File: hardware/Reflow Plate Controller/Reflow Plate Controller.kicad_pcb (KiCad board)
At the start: 4 copper layers, 95 x 43 mm, 86 parts, among them J1 SWD, J2 USB_C_Receptacle_USB2.0_16P, J3 JST-XH, J4 OLED, J5 XT30, J6 XT30, Q1 AO4262E, Q2 SUD50P06-15, Q3 BSS138, SW1 SW_SPST, SW2 SW_SPST, SW3 SW_SPST, SW4 SW_SPST, SW5 SW_SPST, SW6 SW_SPST, SW7 SW_SPST, U1 L78L12ABU, U2 TPS560430, U3 STM32G431KBTx, U4 D5V0P4UR6SO-7, U5 TPD6S300A, U6 UCC27511ADBV

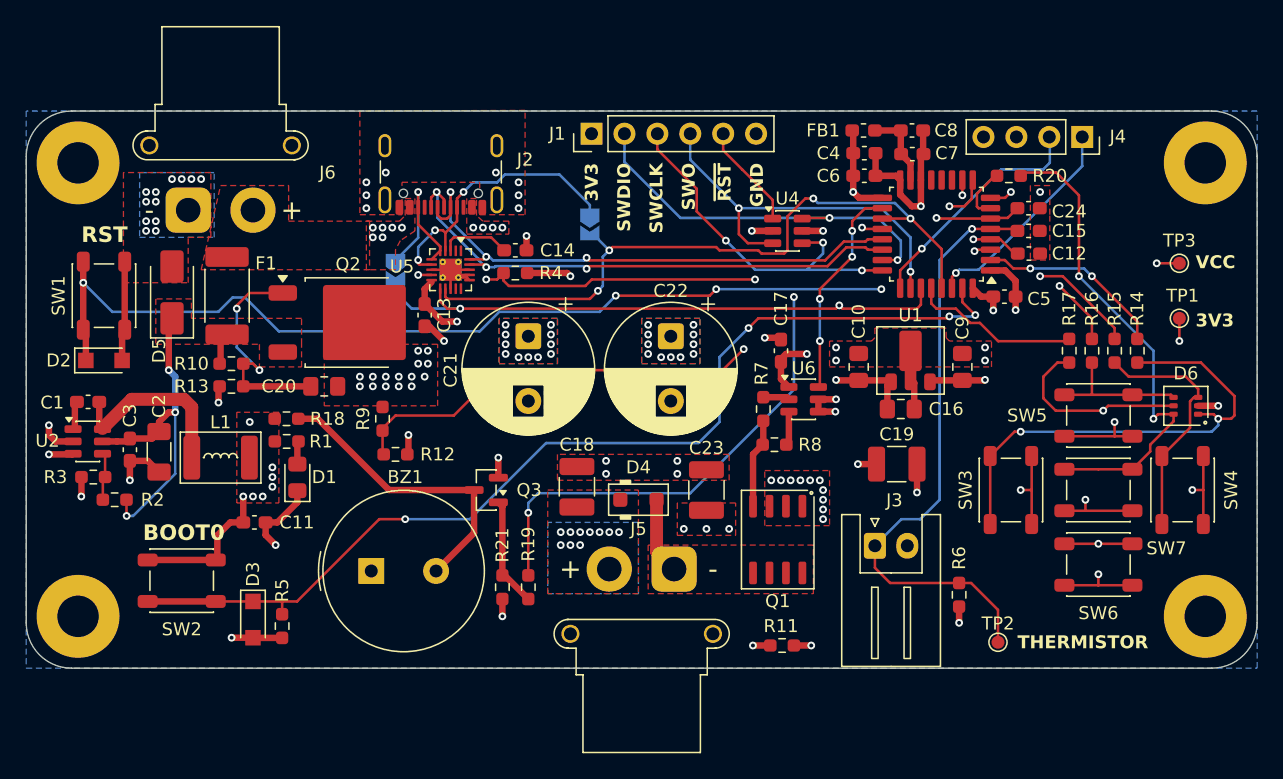
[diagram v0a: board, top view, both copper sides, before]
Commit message: Fix a few layout and component selection issues
- Replace out-of-stock components
- Remove some of the 100nF caps that are in parallel with a larger value
- Swap PTVS3V3 -> SD03
- Swap the PMOS to HSU6119 and the NMOS to DOD130N06 for lower Rds(on)
- Slightly increase the copper area around the FETs
- Reduce the soft-start duration to 47 ms
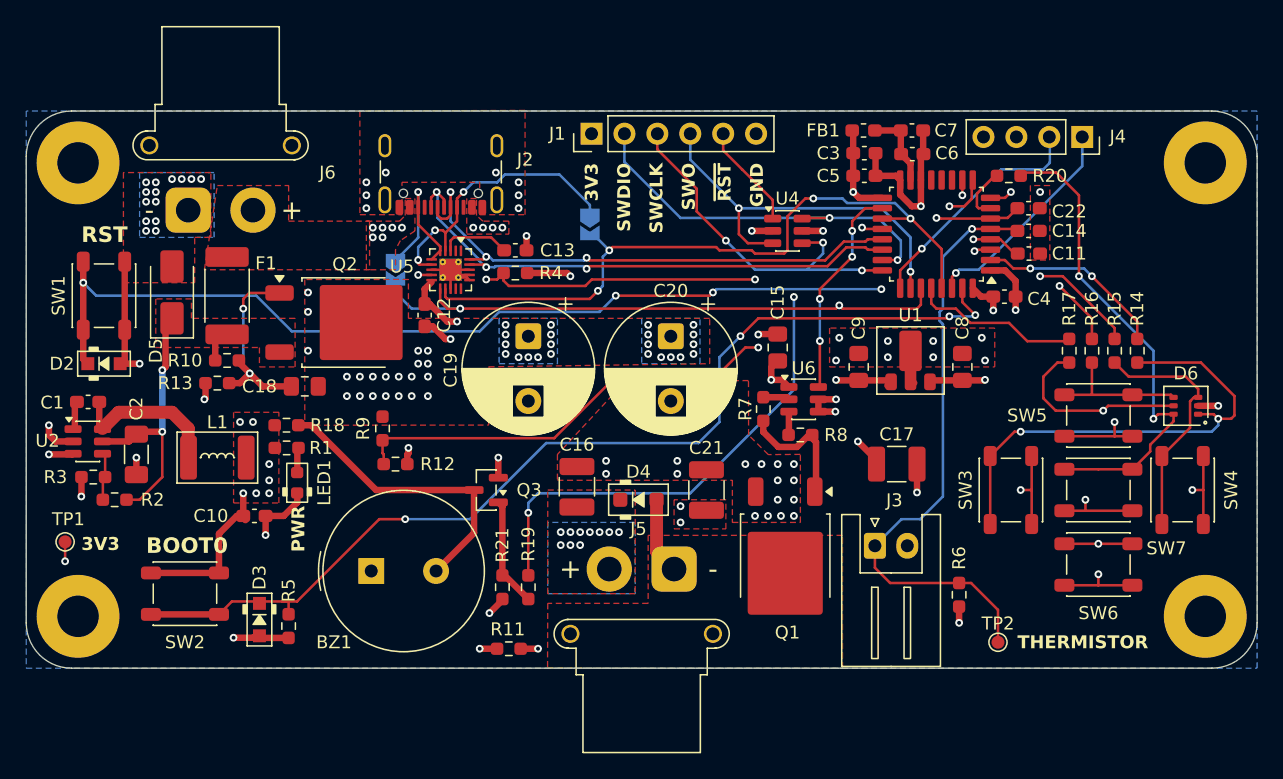
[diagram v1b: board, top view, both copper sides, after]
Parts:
- removed the C16 at (166.0, 101.2)
- removed the C17 at (156.8, 96.8)
- removed the C3 at (106.5, 104.4)
- removed D1: RED, LED_SMD:LED_0805_2012Metric_Pad1.15x1.40mm_HandSolder
- removed TP3: TestPoint, TestPoint:TestPoint_Pad_D1.0mm
- added C15: 2.2u, Capacitor_SMD:C_0805_2012Metric_Pad1.18x1.45mm_HandSolder, F.Cu at (156.5, 96.5)
- added LED1: LED_0603_Red, PCM_LED_SMD_AKL:LED_0603_1608Metric, F.Cu at (119.4, 106.9)
- C18: renamed from C20; value 2.2u -> 1u
- D2, D3: value PTVS3V3S1UR -> SD03; footprint Diode_SMD:Nexperia_CFP3_SOD-123W -> PCM_Diode_SMD_AKL:D_SOD-323_HandSoldering
- D4: footprint PCM_Diode_SMD_AKL:D_SOD-123F -> PCM_Diode_SMD_Handsoldering_AKL:D_SOD-123F
- Q1: value AO4262E -> DOD130N06; footprint PCM_Package_SO_AKL:SO-8_3.9x4.9mm_P1.27mm -> Package_TO_SOT_SMD:TO-252-2
- Q2: value SUD50P06-15 -> HSU6119
- moved TP1 87.7 mm to (101.5, 111.5)
- moved R11 21.1 mm to (135.8, 119.8)
- moved R8 2.14 mm to (158.2, 103.2), turned to 0 degrees
- moved C2 1.76 mm to (107.0, 104.8)
- moved C18 1.50 mm to (120.0, 99.5)
- moved Q1 1.46 mm to (157.1, 112.7)
- moved R13 1.12 mm to (113.2, 99.2)
- moved SW2 1.03 mm to (110.8, 115.5)
- moved R12 0.75 mm to (127.0, 105.5)
- moved R9 0.75 mm to (126.0, 102.8)
- moved C10 0.50 mm to (116.1, 109.5)
- moved D3 0.50 mm to (116.5, 117.5)
- moved R1 0.50 mm to (118.6, 104.2)
- moved R18 0.50 mm to (118.6, 102.5)
- moved R5 0.50 mm to (118.8, 118.0)
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- renumbered C11 to C10, C12 to C11, C13 to C12, C14 to C13, C15 to C14, C18 to C16, C19 to C17, C21 to C19, C22 to C20, C23 to C21, C24 to C22, C4 to C3, C5 to C4, C6 to C5, C7 to C6, C8 to C7, C9 to C8, C10 to C9
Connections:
- Q1 pad 1: GND -> Net-(Q1-G)
- Q1 pad 2: GND -> /PLATE_GND
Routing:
- net VBUSP: track 28.1 -> 23.0 mm, vias 3 -> 2
- net GND: track 71.6 -> 68.6 mm, vias 81 -> 90
- net Net-(Q1-G): track 6.92 -> 9.91 mm
- net Net-(Q2-G): track 18.1 -> 15.8 mm
- net Net-(U2-SW): track 14.2 -> 12.1 mm
- net +12V: track 14.2 -> 13.0 mm
- net VCC: track 8.84 -> 8.00 mm, vias 54 -> 58
- net Net-(U6-OUTL): track 2.63 -> 1.81 mm
- net /BOOT0: track 79.4 -> 80.1 mm
- net +3V3: track 72.1 -> 72.7 mm
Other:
- board text added: "PWR"
- board text removed: "VCC"
